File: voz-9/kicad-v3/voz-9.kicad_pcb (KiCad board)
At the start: 2 copper layers, 200 x 100 mm, 232 parts, among them J1 AMOUNT, J1 CUTOFF, J1 DRONE, J1 OSC A, J1 OSC B, J1 SHAPE, J1 SW A, J1 SW B, J2 DEPTH, J2 MODE, J2 RATE, J2 TREM, J3 F-BACK, J3 H1, J3 H2, J3 H3, J3 STACK, J3 TIME, J3 VOLUME, J3 WET, J4 A, J4 B, J4 FCV, J4 FILT, J4 IN, J4 VCV, J5 CLK, J5 ECV, J5 LFO, J5 RCV, J5 SEND, J6 GATE, J6 LED, J6 P4, J7 OSC IN, J7 PRE, J7 XLR IN, J8 XLR OUT, J9 HIGH, J9 LOW, J9 MID F, J9 MID G, Q1 MMBFJ201, Q2 MMBFJ201, Q3 MMBFJ201, Q4 MMBFJ201, Q5 MMBFJ201, Q6 MMBFJ201, Q7 MMBF5457, U1 NE5532DR, U2 TL072CDR, U3 TL072CDR, U4 ICL7660, U5 78M05, U6 PT2399, U7 PT2399, U8 PT2399, U9 TL072CDR

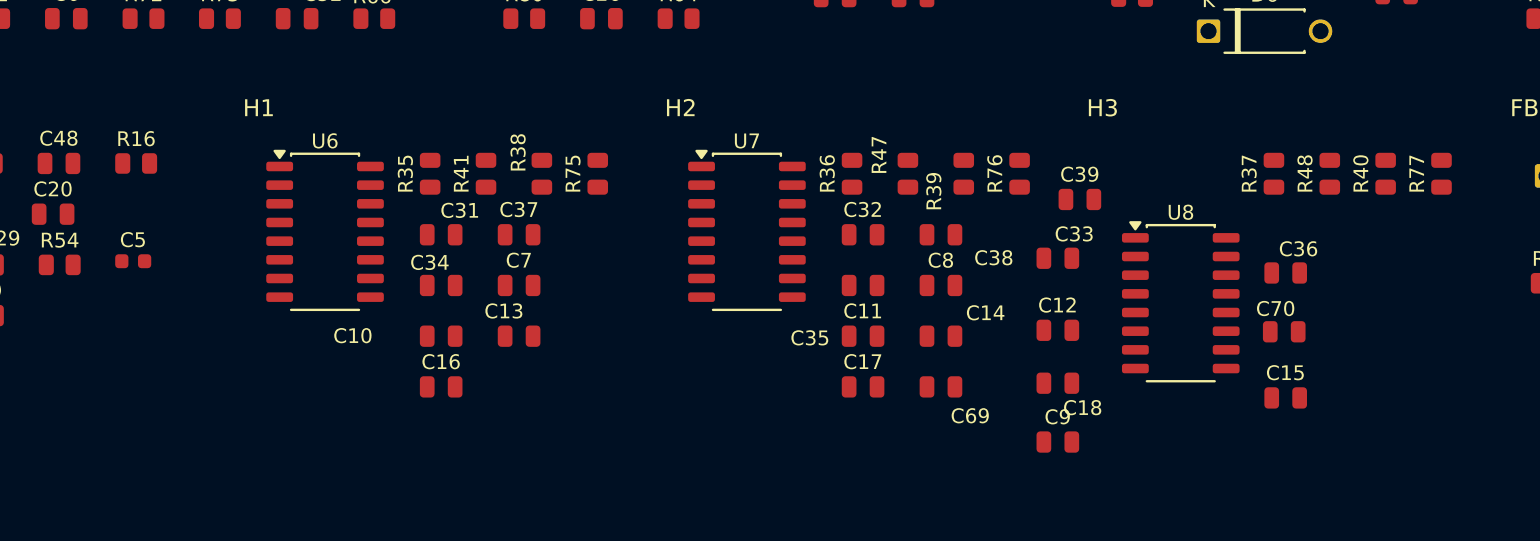
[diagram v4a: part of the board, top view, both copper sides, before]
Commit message: Copia o arranjo do H3 para os passivos de H1 e H2.
Resistores em cima do PT2399, capacitores dos dois lados e o resistor de 220k embaixo.

Co-authored-by: Andrey <andreysenes@users.noreply.github.com>
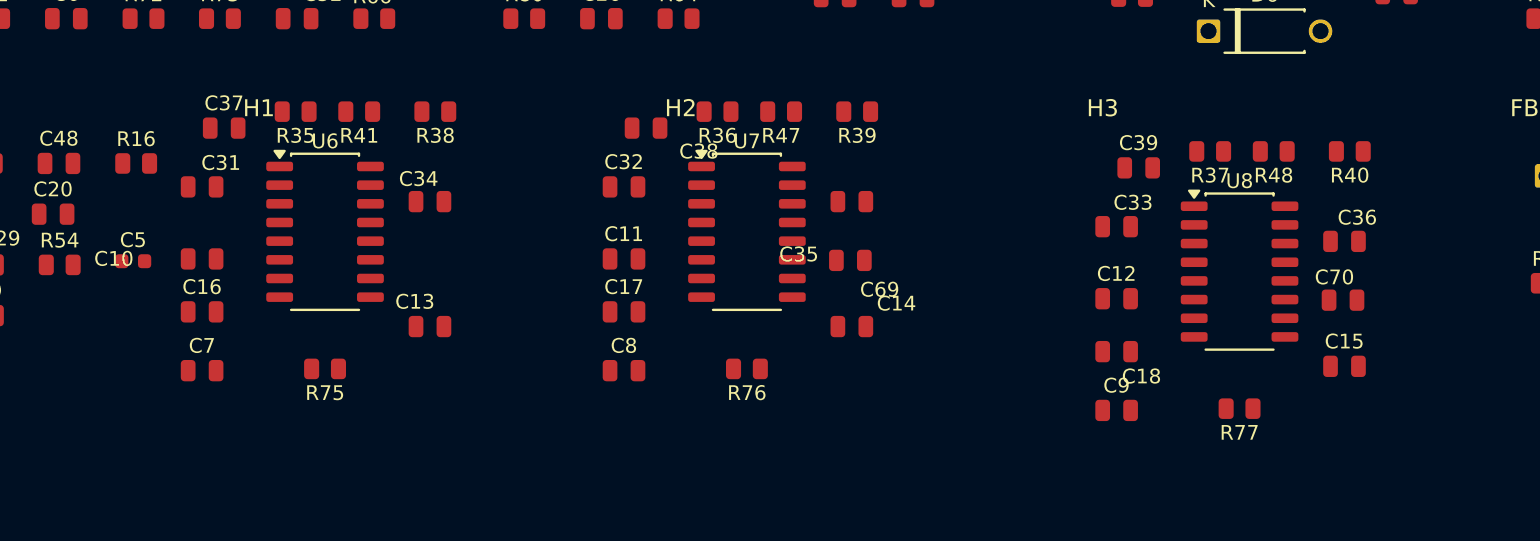
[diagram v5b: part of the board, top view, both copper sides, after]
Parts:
- moved R75 22.8 mm to (47.7, 51.5), turned to 180 degrees
- moved R76 22.8 mm to (76.4, 51.5), turned to 180 degrees
- moved C7 22.3 mm to (39.3, 51.6)
- moved C8 22.3 mm to (68.0, 51.6)
- moved C37 21.3 mm to (40.8, 35.1)
- moved C38 21.3 mm to (69.5, 35.1)
- moved R77 21.1 mm to (109.9, 54.2), turned to 180 degrees
- moved C10 17.1 mm to (39.3, 44.0)
- moved C11 17.1 mm to (68.0, 44.0)
- moved C16 17.0 mm to (39.3, 47.6)
- moved C17 17.0 mm to (68.0, 47.6)
- moved C31 16.6 mm to (39.3, 39.1)
- moved C32 16.6 mm to (68.0, 39.1)
- moved C69 10.6 mm to (83.4, 44.1)
- moved R35 10.1 mm to (45.7, 34.0), turned to 180 degrees
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
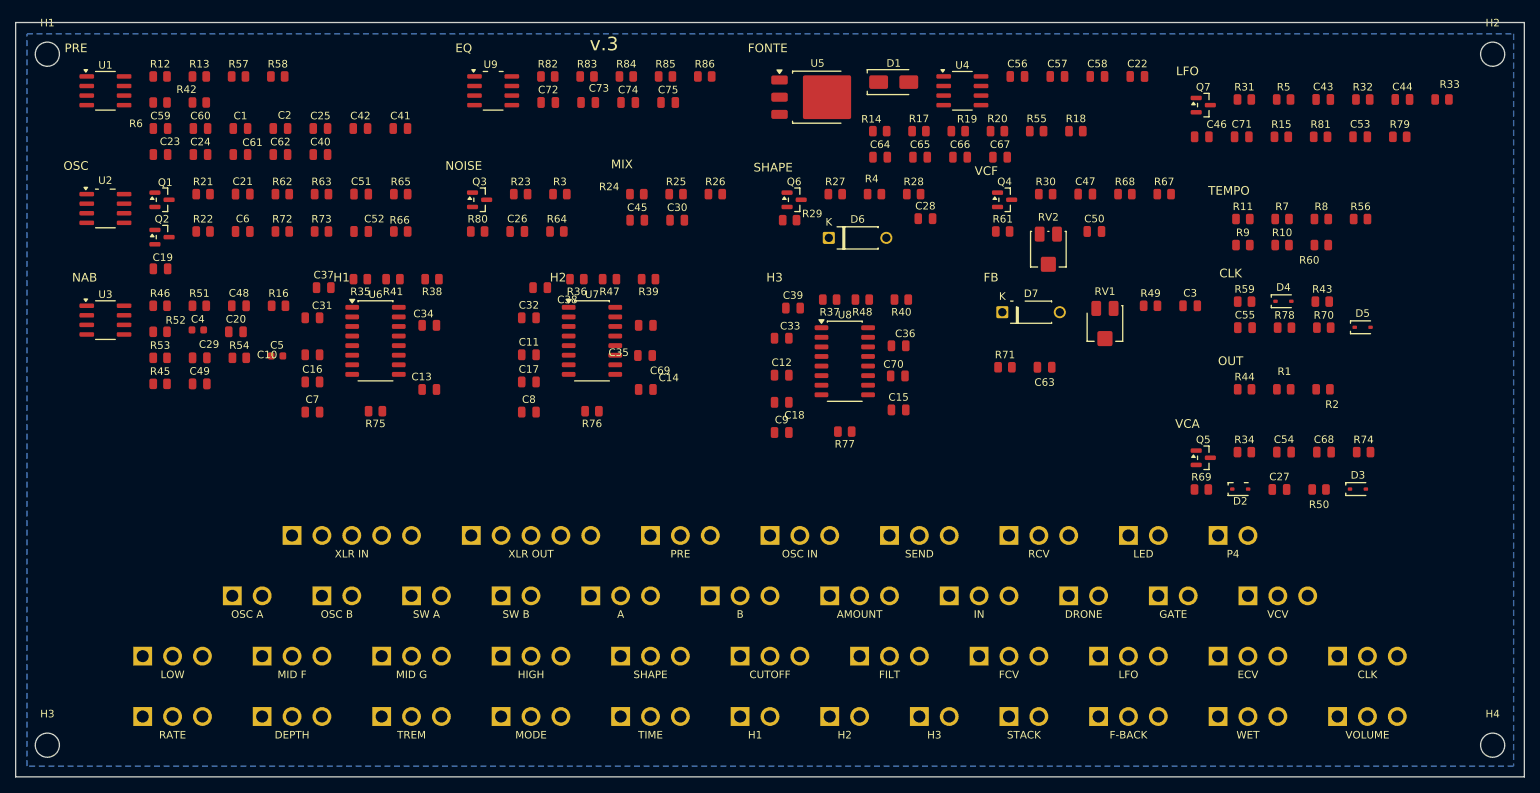
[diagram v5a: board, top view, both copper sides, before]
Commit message: Organiza os grupos da v3 numa grade simétrica de 5,2 mm.
PRE, EQ, FONTE, OSC, NOISE, MIX, SHAPE, VCF, NAB, H1–H3 e FB ficam com o mesmo passo, espelhados em volta do CI. A coluna LFO/TEMPO/CLK/OUT/VCA e os pinos da base não se movem.

Co-authored-by: Andrey <andreysenes@users.noreply.github.com>
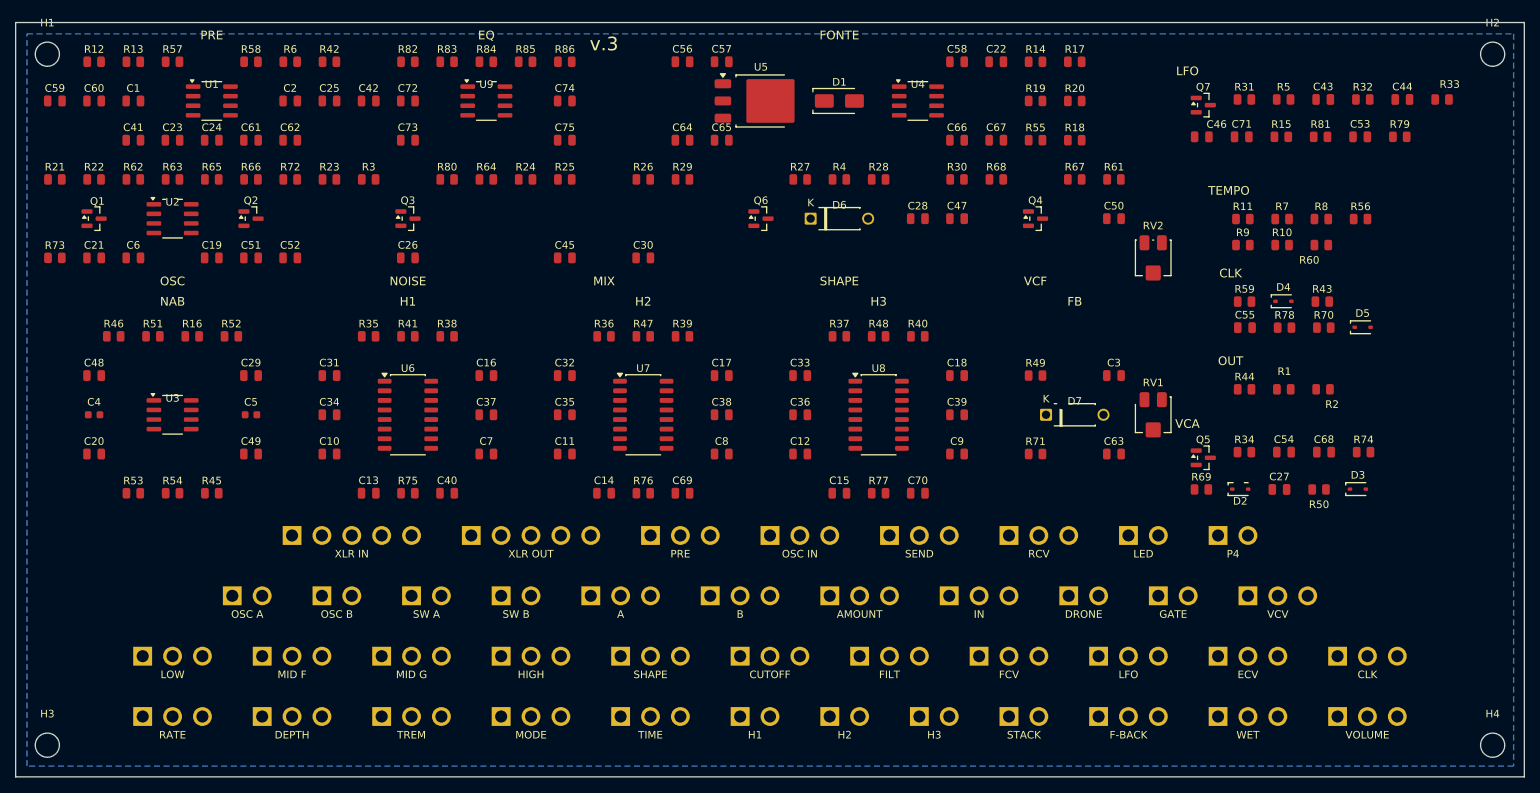
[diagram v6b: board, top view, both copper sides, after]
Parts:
- moved C40 47.9 mm to (57.2, 62.4)
- moved C57 44.5 mm to (93.6, 5.20)
- moved C56 44.4 mm to (88.4, 5.20)
- moved R73 35.5 mm to (5.20, 31.2)
- moved C41 35.4 mm to (15.6, 15.6)
- moved C38 29.4 mm to (93.6, 52.0)
- moved C37 27.4 mm to (62.4, 52.0)
- moved C65 26.4 mm to (93.6, 15.6)
- moved C64 26.3 mm to (88.4, 15.6)
- moved C8 26.2 mm to (93.6, 57.2)
- moved C39 25.9 mm to (124.8, 52.0)
- moved C17 25.6 mm to (93.6, 46.8)
- moved R3 25.4 mm to (46.8, 20.8)
- moved R23 25.4 mm to (41.6, 20.8)
- moved R65 25.1 mm to (26.0, 20.8)
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
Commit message: Aproxima os grupos da v3 e recolhe as peças que ficaram no vão.
PRE, EQ, FONTE, OSC, NOISE, MIX, SHAPE e VCF ficam encostados no passo de 5,2 mm, com as filas contínuas. O RV2 entra na fila do VCF e os resistores da fonte acompanham o bloco.

Co-authored-by: Andrey <andreysenes@users.noreply.github.com>
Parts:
- moved C42 31.6 mm to (15.6, 15.6)
- moved RV2 16.4 mm to (135.2, 26.0)
- moved C56 15.6 mm to (72.8, 5.20)
- moved C64 15.6 mm to (72.8, 15.6)
- moved D1 15.6 mm to (93.6, 10.4)
- moved R17 15.6 mm to (124.8, 5.20)
- moved R18 15.6 mm to (124.8, 15.6)
- moved R20 15.6 mm to (124.8, 10.4)
- moved R28 15.6 mm to (98.8, 20.8)
- moved R4 15.6 mm to (93.6, 20.8)
- moved R67 15.6 mm to (124.8, 20.8)
- moved C22 15.6 mm to (114.4, 5.20)
- moved C28 15.6 mm to (104.0, 26.0)
- moved C47 15.6 mm to (109.2, 26.0)
- moved C50 15.6 mm to (130.0, 26.0)
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
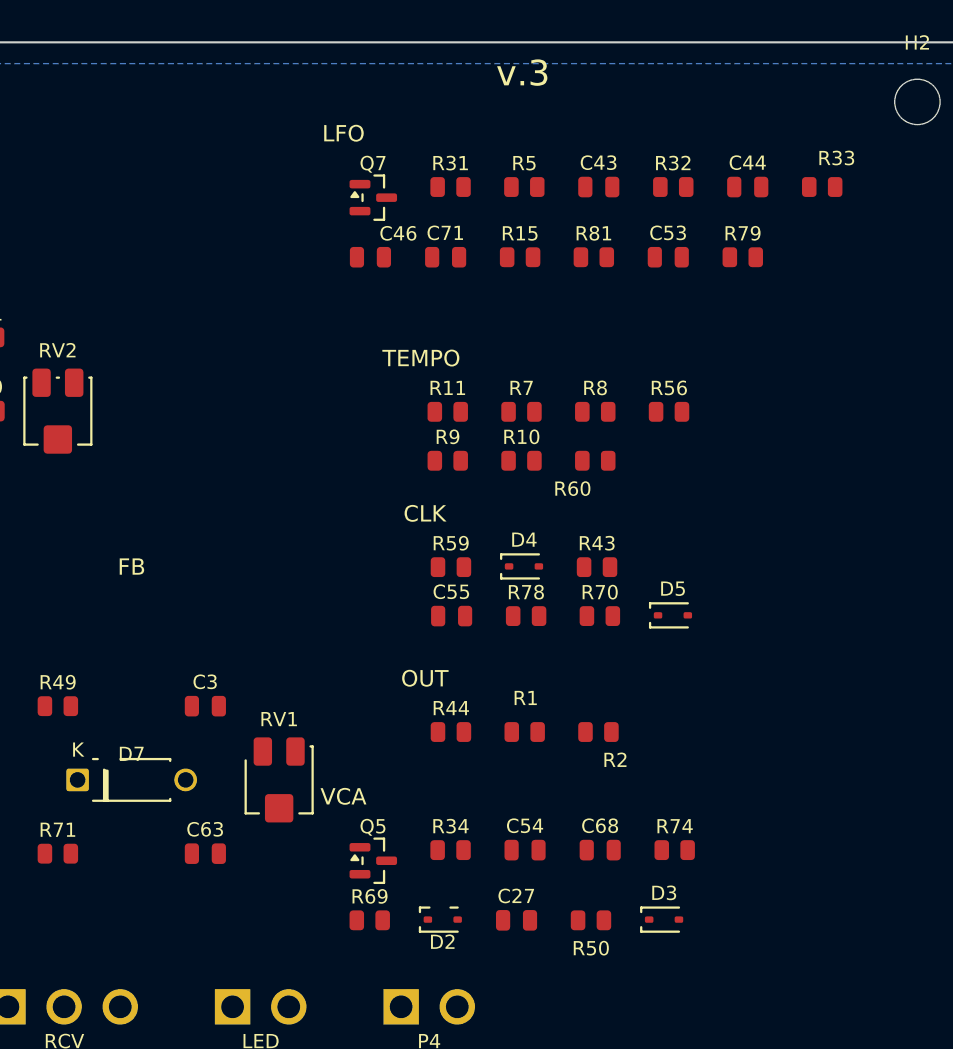
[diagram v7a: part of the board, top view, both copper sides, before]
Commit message: Padroniza LFO, TEMPO, CLK, OUT e VCA no passo de 5,2 mm.
Os cinco blocos ficam na mesma coluna, centrados no mesmo eixo, com filas simétricas. TEMPO e CLK repetem a figura de quatro sobre três; o VCA repete as duas filas de cinco.

Co-authored-by: Andrey <andreysenes@users.noreply.github.com>
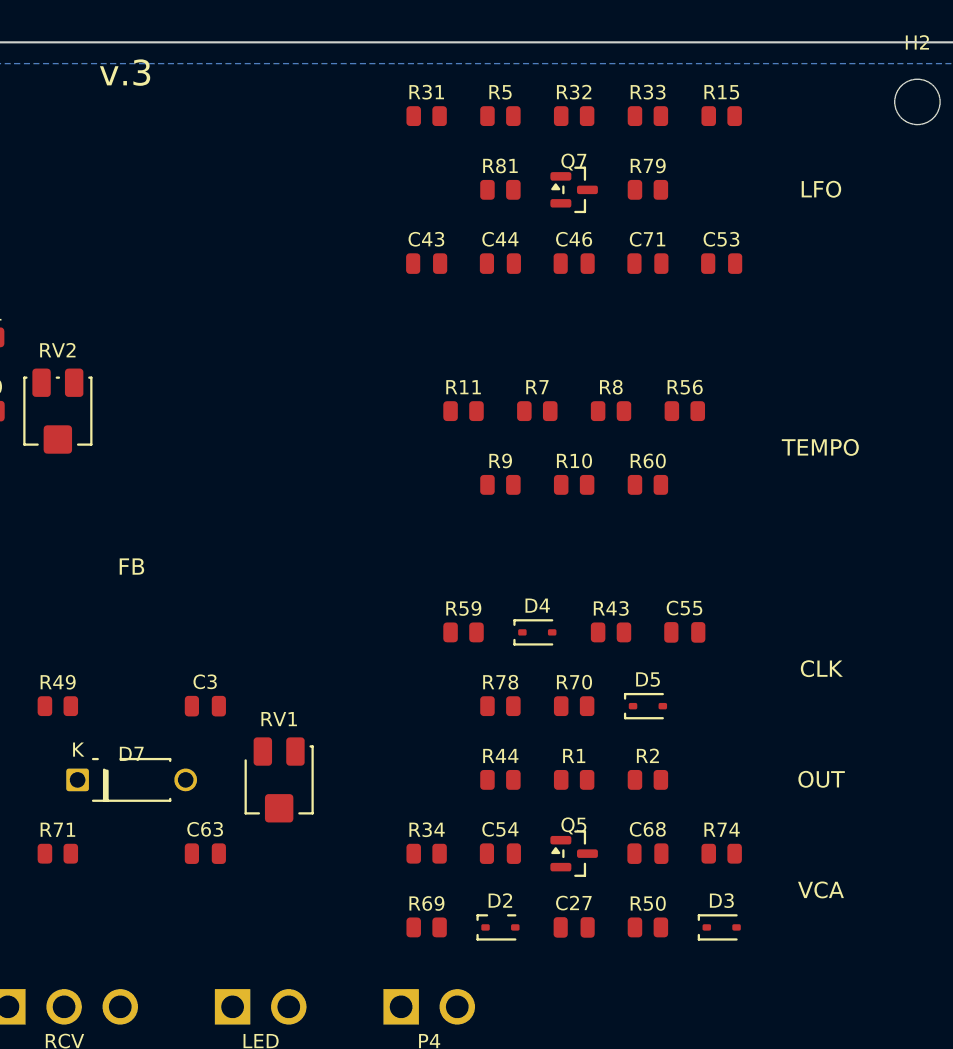
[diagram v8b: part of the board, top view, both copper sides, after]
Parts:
- moved C44 18.3 mm to (166.4, 15.6)
- moved R15 17.3 mm to (182.0, 5.20)
- moved C55 16.5 mm to (179.4, 41.6)
- moved C46 14.4 mm to (171.6, 15.6)
- moved C71 14.3 mm to (176.8, 15.6)
- moved Q7 14.2 mm to (171.6, 10.4)
- moved Q5 14.2 mm to (171.6, 57.2)
- moved C43 13.3 mm to (161.2, 15.6)
- moved R33 13.3 mm to (176.8, 5.20)
- moved R32 8.59 mm to (171.6, 5.20)
- moved R79 8.20 mm to (176.8, 10.4)
- moved R81 8.12 mm to (166.4, 10.4)
- moved D5 6.64 mm to (176.8, 46.8)
- moved R70 6.60 mm to (171.6, 46.8)
- moved R78 6.60 mm to (166.4, 46.8)
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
